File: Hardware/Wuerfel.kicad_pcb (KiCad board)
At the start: 2 copper layers, 17 parts, among them SW1 SW_Push, U1 ATTINY13A-PU

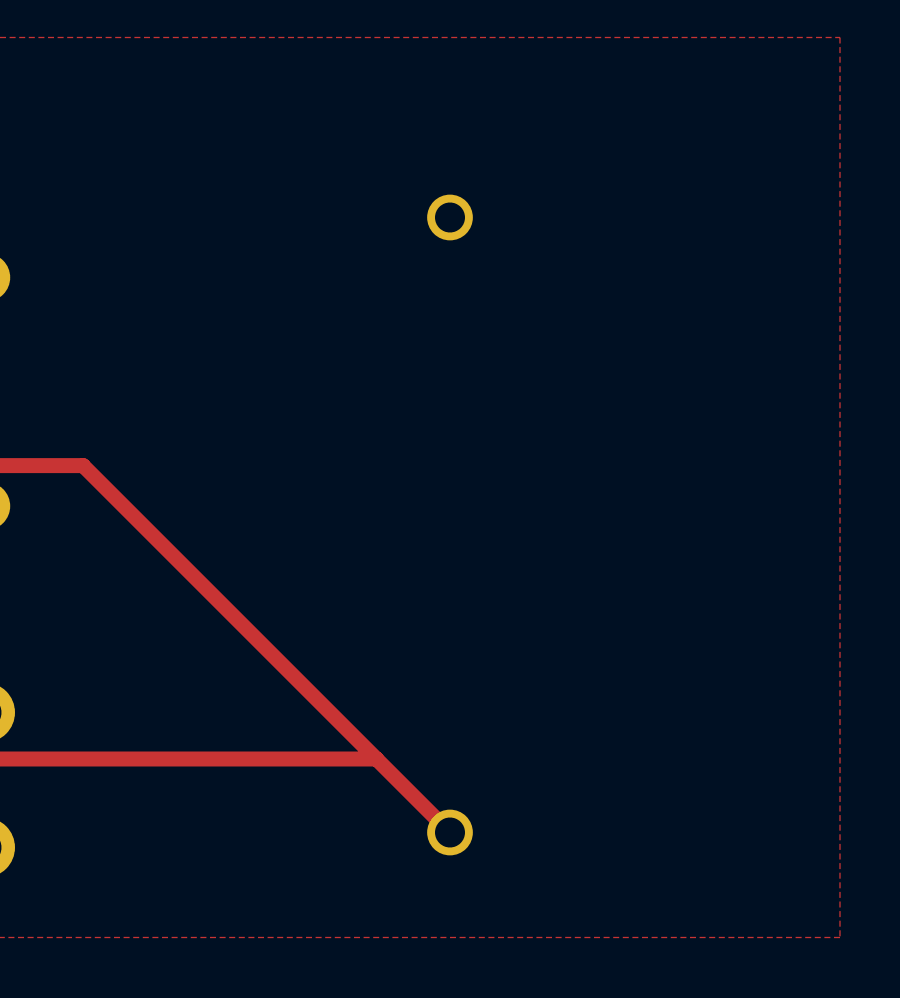
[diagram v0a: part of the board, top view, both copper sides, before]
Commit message: Migrated to KiCAD 5.0; Changed drill diameter of KZH20-1
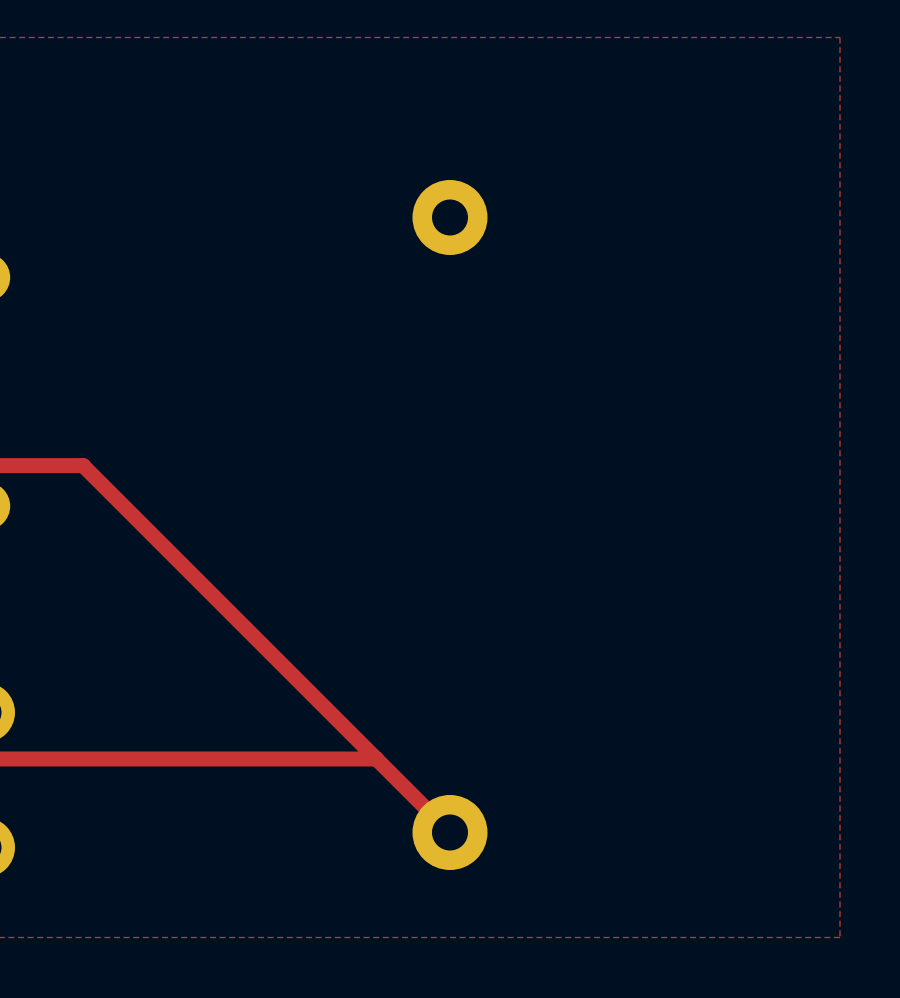
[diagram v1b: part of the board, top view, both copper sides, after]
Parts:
- D1, D2, D3, D4, D5, D6, D7: footprint LEDs:LED_D5.0mm -> LED_THT:LED_D5.0mm
- R1, R2, R3, R4, R5, R6, R7: footprint Resistors_THT:R_Axial_DIN0207_L6.3mm_D2.5mm_P10.16mm_Horizontal -> Resistor_THT:R_Axial_DIN0207_L6.3mm_D2.5mm_P10.16mm_Horizontal
- SW1: footprint Buttons_Switches_THT:SW_PUSH_6mm_h7.3mm -> Button_Switch_THT:SW_PUSH_6mm_H7.3mm
- U1: footprint Housings_DIP:DIP-8_W7.62mm -> Package_DIP:DIP-8_W7.62mm
